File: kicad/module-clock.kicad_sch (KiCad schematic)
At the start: 23 parts, among them SW1 SW_Push, SW2 SW_SPDT, U1 NE555P, U2 NE555P, U3 NE555P

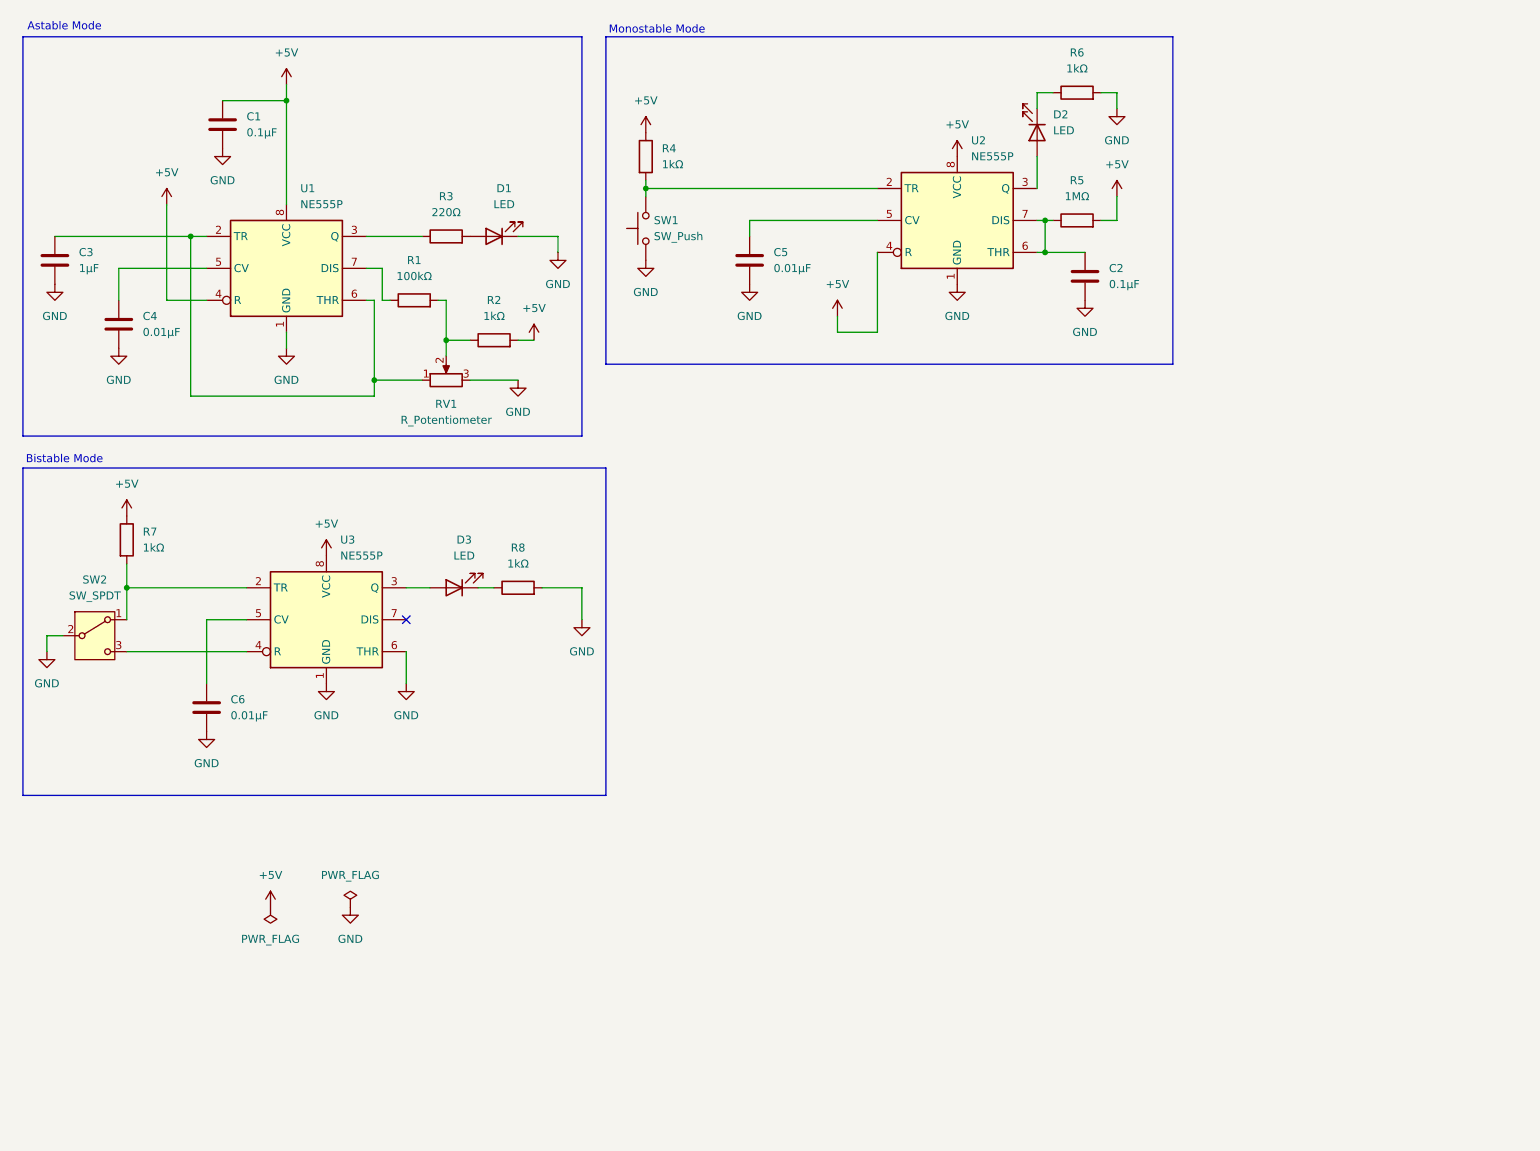
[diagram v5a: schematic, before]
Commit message: Add clock logic
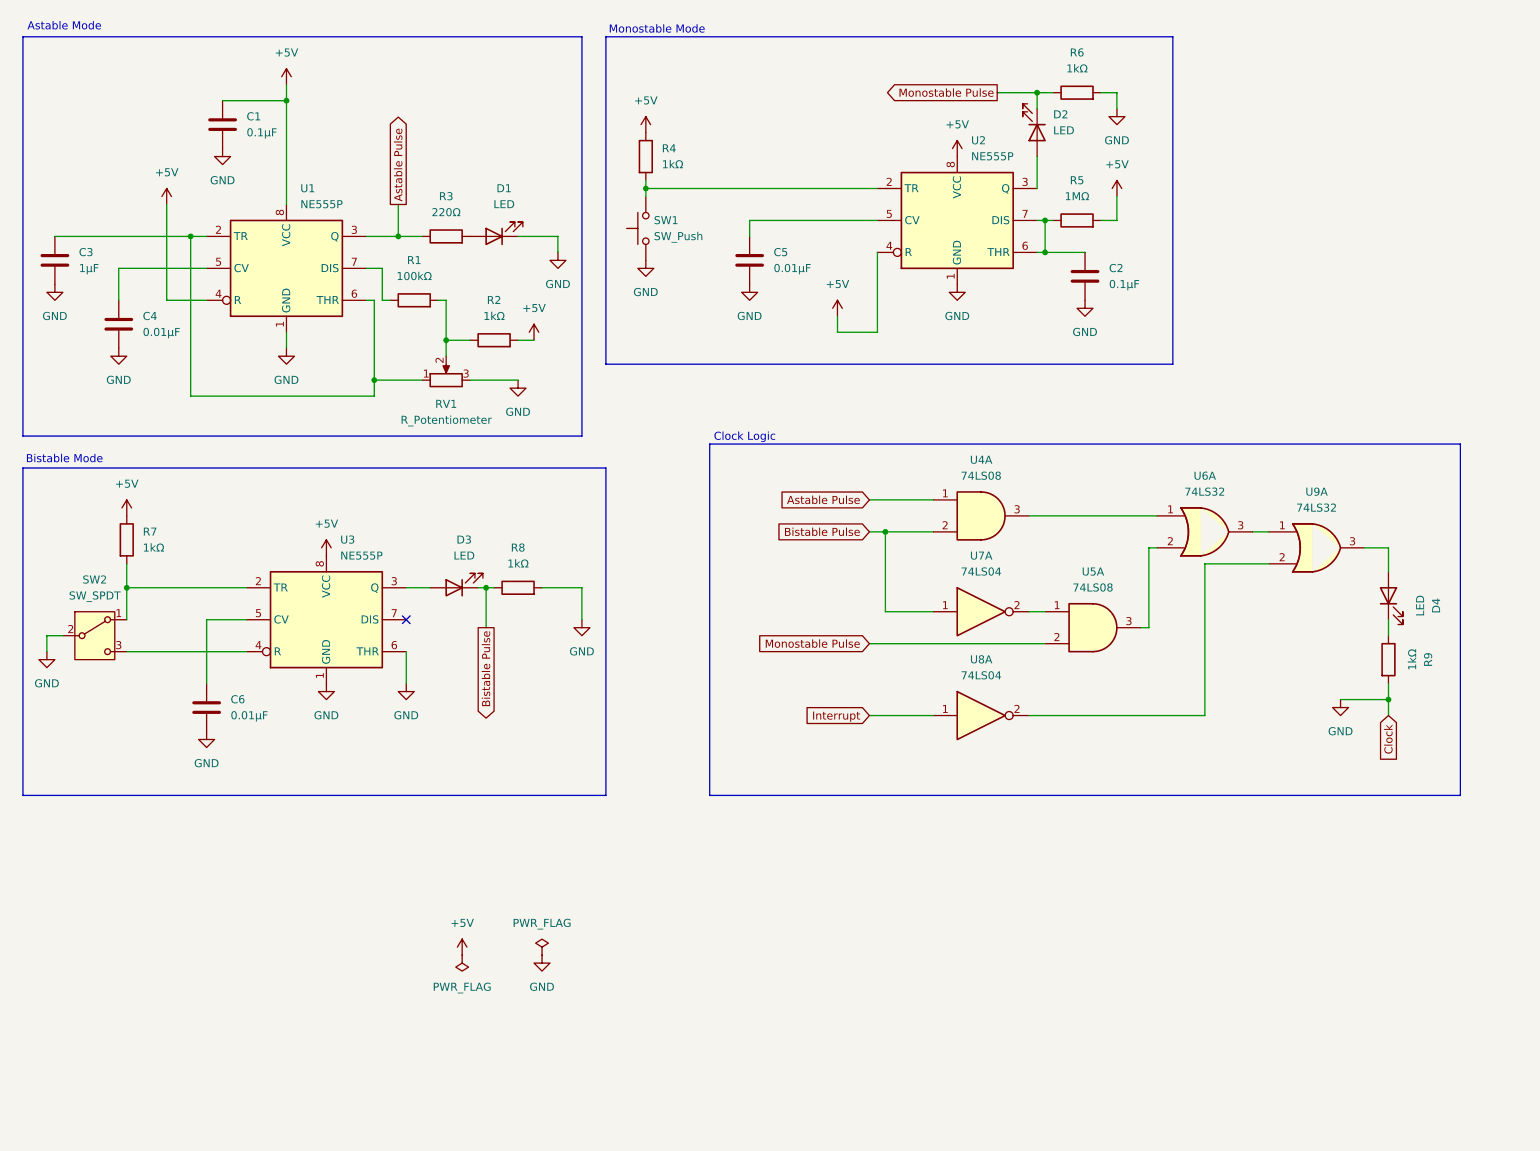
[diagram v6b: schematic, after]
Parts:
- added D4: LED, symbol Device:LED
- added R9: 1kΩ, symbol Device:R
- added U4, U5: 74LS08, symbol 74xx:74LS08
- added U6, U9: 74LS32, symbol 74xx:74LS32
- added U7, U8: 74LS04, symbol 74xx:74LS04
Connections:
- net GND: now also R9.2
- net Bistable Pulse: now reaches D3.1 (K), R8.1
- net Bistable Pulse: now also U4.2, U7.1
- net Astable Pulse: now reaches R3.1, U1.3 (Q)
- net Astable Pulse: now also U4.1
- net Monostable Pulse: now reaches D2.1 (K), R6.1
- net Monostable Pulse: now also U5.2
- new net: U6.3, U9.1
- new net: U8.2, U9.2
- new net: D4.2 (A), U9.3
- new net: U5.1, U7.2
- new net: U4.3, U6.1
- new net: U5.3, U6.2
- new net: D4.1 (K), R9.1
- new net Interrupt: U8.1
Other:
- note added: "Clock Logic"

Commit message: Remove LED status
Remove debugging LED and use a main one depending on selected state
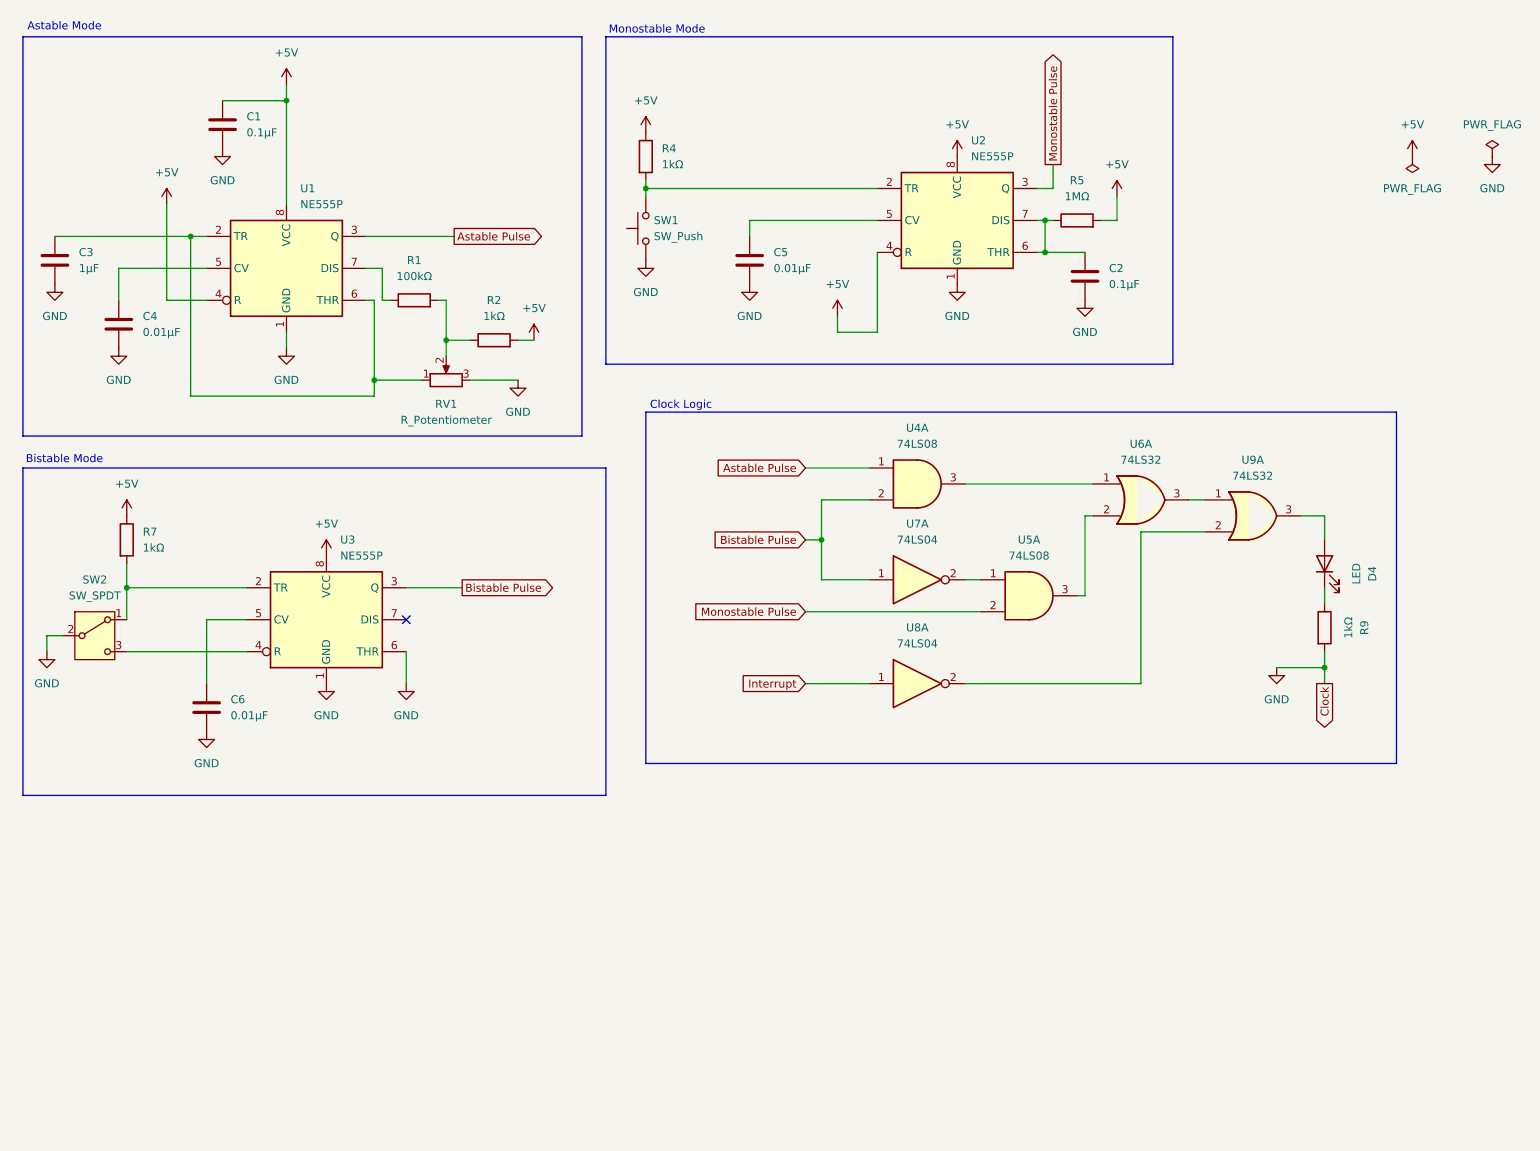
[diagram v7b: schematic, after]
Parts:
- removed D1, D2, D3: LED, symbol Device:LED
- removed R3: 220Ω, symbol Device:R
- removed R6, R8: 1kΩ, symbol Device:R
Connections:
- net Bistable Pulse: now also U3.3 (Q)
- net Monostable Pulse: now also U2.3 (Q)
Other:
- moved on the sheet: D4, R9, U4A, U5A, U6A, U7A, U8A, U9A

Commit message: Update astable clock mode
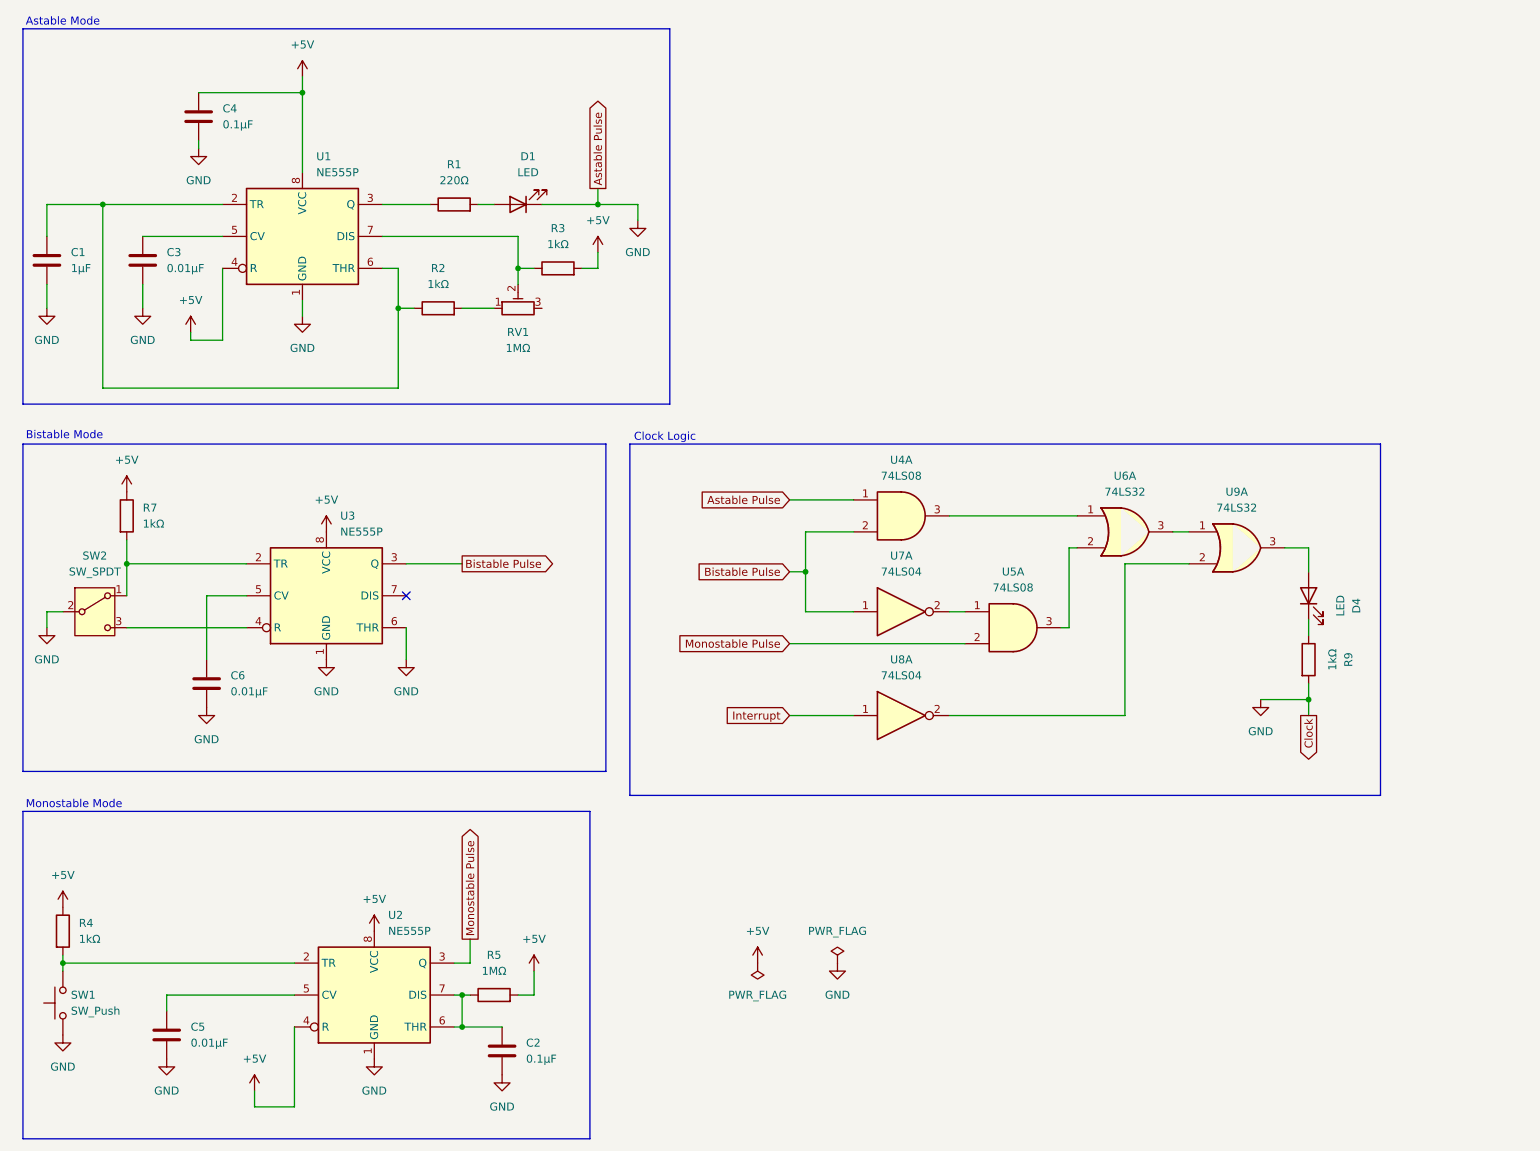
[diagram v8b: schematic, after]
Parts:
- removed RV1: R_Potentiometer, symbol Device:R_Potentiometer
- added D1: LED, symbol Device:LED
- added R3: 1kΩ, symbol Device:R
- added RV1: 1MΩ, symbol Device:R_Potentiometer_Trim
- C1: value 0.1μF -> 1μF
- C3: value 1μF -> 0.01μF
- C4: value 0.01μF -> 0.1μF
- R1: value 100kΩ -> 220Ω
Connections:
- net +5V: now also C4.1, R3.2; no longer C1.1, R2.2
- net GND: now also U4.1, D1.1 (K)
- net at R2.1: now also C1.1, U1.2 (TR), U1.6 (THR); no longer R1.2
- net at U1.5 (CV): now also C3.1; no longer C4.1
- net at U1.7 (DIS): now also R3.1, RV1.2; no longer R1.1
- net Astable Pulse: no longer names the net of U1.3 (Q)
- net Astable Pulse: now also R1.1; no longer U4.1
- new net: R2.2, RV1.1
- new net: D1.2 (A), R1.2
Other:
- moved on the sheet: C2, C5, C6, D4, R4, R5, R7, R9, SW1, SW2, U2, U3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
